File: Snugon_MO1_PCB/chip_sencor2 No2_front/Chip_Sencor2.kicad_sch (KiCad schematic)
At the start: 7 parts, among them J4 Conn_01x8_Pin + 2, SW12 RotaryEncoder, SW2 SW_PUSH, SW3 SW_PUSH, SW4 SW_PUSH, SW5 SW_PUSH, SW6 SW_PUSH

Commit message: スイッチとエンコーダーはPCBAしない
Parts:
- SW12: LCSC C400278 -> (none)
- SW2, SW3, SW4, SW5, SW6: LCSC C400268 -> (none)
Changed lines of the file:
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@@
       (effects (font (size 1.27 1.27)))
     )
-    (property "LCSC" "C400268" (at 146.05 90.17 0)
+    (property "LCSC" "" (at 146.05 90.17 0)
       (effects (font (size 1.27 1.27)) hide)
     )
@@
       (effects (font (size 1.27 1.27)))
     )
-    (property "LCSC" "C400268" (at 146.05 105.41 0)
+    (property "LCSC" "" (at 146.05 105.41 0)
       (effects (font (size 1.27 1.27)) hide)
     )
@@
       (effects (font (size 1.27 1.27)))
     )
-    (property "LCSC" "C400268" (at 146.05 120.65 0)
+    (property "LCSC" "" (at 146.05 120.65 0)
       (effects (font (size 1.27 1.27)) hide)
     )
@@
       (effects (font (size 1.27 1.27)))
     )
-    (property "LCSC" "C400268" (at 146.05 74.93 0)
+    (property "LCSC" "" (at 146.05 74.93 0)
       (effects (font (size 1.27 1.27)) hide)
     )
@@
       (effects (font (size 1.27 1.27)))
     )
-    (property "LCSC" "C400268" (at 146.05 59.69 0)
+    (property "LCSC" "" (at 146.05 59.69 0)
       (effects (font (size 1.27 1.27)) hide)
     )
@@
       (effects (font (size 1.27 1.27)) hide)
     )
-    (property "LCSC" "C400278" (at 218.44 87.63 0)
-      (effects (font (size 1.27 1.27)) hide)
-    )
+    (property "LCSC" "" (at 218.44 87.63 0)
+      (effects (font (size 1.27 1.27)) hide)
+    )

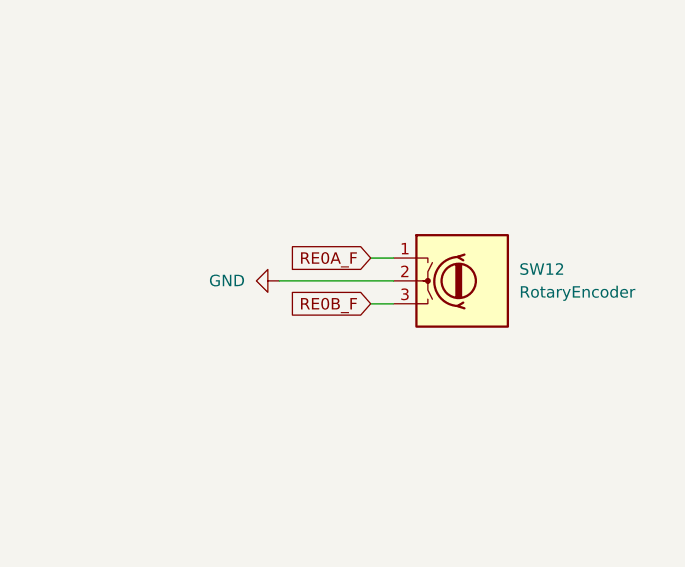
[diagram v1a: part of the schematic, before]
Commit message: エンコーダの配線修正
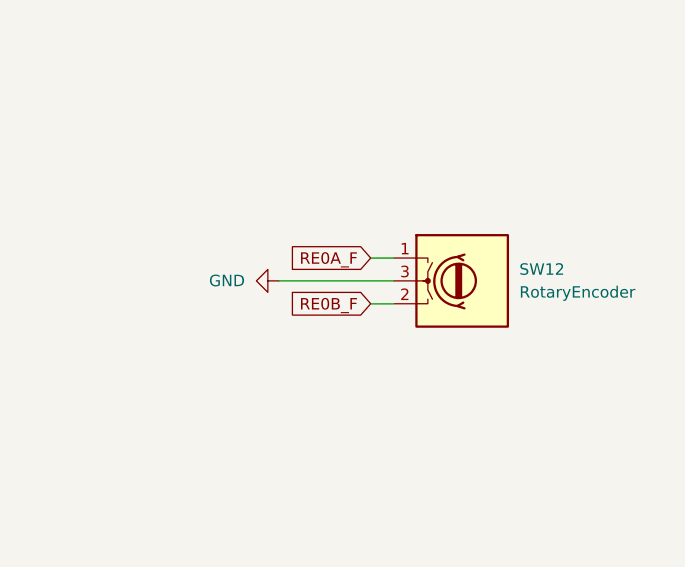
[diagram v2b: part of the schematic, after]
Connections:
- net GND: now also SW12.3; no longer SW12.2
- net RE0B_F: now also SW12.2; no longer SW12.3
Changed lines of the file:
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@@
     )
     (pin "1")
+    (pin "3")
     (pin "2")
-    (pin "3")
     (instances
       (project "Chip_Sencor2"
